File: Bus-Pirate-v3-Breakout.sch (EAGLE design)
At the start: 9 parts

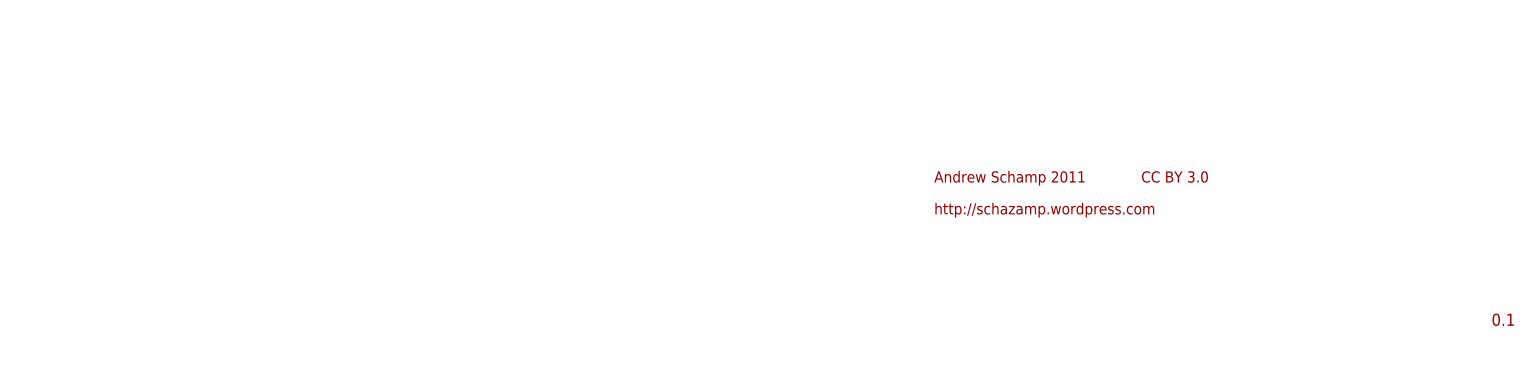
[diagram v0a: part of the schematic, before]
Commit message: Clean up and add panelization config
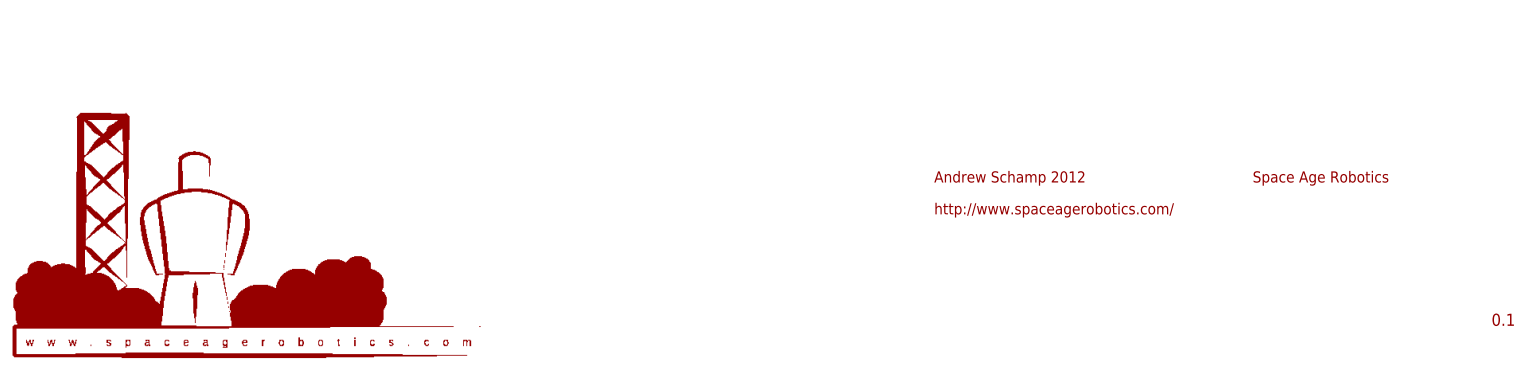
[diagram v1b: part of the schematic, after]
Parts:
- added U$2: LOGO_SPACE_AGE_ROBOTICS0.48*0.27, logos:LOGO_SPACE_AGE_ROBOTICS0.48*0.27
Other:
- note added: "Andrew Schamp 2012"
- note added: "Space Age Robotics"
- note added: "http://www.spaceagerobotics.com/"
- note removed: "Andrew Schamp 2011"
- note removed: "CC BY 3.0"
- note removed: "http://schazamp.wordpress.com"
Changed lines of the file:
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@@
 <grid distance="0.1" unitdist="inch" unit="inch" style="lines" multiple="1" display="no" altdistance="0.01" altunitdist="inch" altunit="inch"/>
 <layers>
-<layer number="1" name="Top" color="4" fill="1" visible="no" active="no"/>
-<layer number="16" name="Bottom" color="1" fill="1" visible="no" active="no"/>
-<layer number="17" name="Pads" color="2" fill="1" visible="no" active="no"/>
-<layer number="18" name="Vias" color="2" fill="1" visible="no" active="no"/>
-<layer number="19" name="Unrouted" color="6" fill="1" visible="no" active="no"/>
-<layer number="20" name="Dimension" color="7" fill="1" visible="no" active="no"/>
-<layer number="21" name="tPlace" color="16" fill="1" visible="no" active="no"/>
-<layer number="22" name="bPlace" color="14" fill="1" visible="no" active="no"/>
-<layer number="23" name="tOrigins" color="15" fill="1" visible="no" active="no"/>
-<layer number="24" name="bOrigins" color="15" fill="1" visible="no" active="no"/>
-<layer number="25" name="tNames" color="7" fill="1" visible="no" active="no"/>
-<layer number="26" name="bNames" color="7" fill="1" visible="no" active="no"/>
-<layer number="27" name="tValues" color="7" fill="1" visible="no" active="no"/>
-<layer number="28" name="bValues" color="7" fill="1" visible="no" active="no"/>
+<layer number="1" name="Top" color="4" fill="1" visible="yes" active="no"/>
+<layer number="16" name="Bottom" color="1" fill="1" visible="yes" active="no"/>
+<layer number="17" name="Pads" color="2" fill="1" visible="yes" active="no"/>
+<layer number="18" name="Vias" color="2" fill="1" visible="yes" active="no"/>
+<layer number="19" name="Unrouted" color="6" fill="1" visible="yes" active="no"/>
+<layer number="20" name="Dimension" color="15" fill="1" visible="yes" active="no"/>
+<layer number="21" name="tPlace" color="16" fill="1" visible="yes" active="no"/>
+<layer number="22" name="bPlace" color="14" fill="1" visible="yes" active="no"/>
+<layer number="23" name="tOrigins" color="15" fill="1" visible="yes" active="no"/>
+<layer number="24" name="bOrigins" color="15" fill="1" visible="yes" active="no"/>
+<layer number="25" name="tNames" color="7" fill="1" visible="yes" active="no"/>
+<layer number="26" name="bNames" color="7" fill="1" visible="yes" active="no"/>
+<layer number="27" name="tValues" color="7" fill="1" visible="yes" active="no"/>
+<layer number="28" name="bValues" color="7" fill="1" visible="yes" active="no"/>
 <layer number="29" name="tStop" color="7" fill="3" visible="no" active="no"/>
 <layer number="30" name="bStop" color="7" fill="6" visible="no" active="no"/>
-<layer number="31" name="tCream" color="11" fill="4" visible="no" active="no"/>
+<layer number="31" name="tCream" color="7" fill="4" visible="no" active="no"/>
 <layer number="32" name="bCream" color="7" fill="5" visible="no" active="no"/>
 <layer number="33" name="tFinish" color="6" fill="3" visible="no" active="no"/>
@@
 <layer number="35" name="tGlue" color="7" fill="4" visible="no" active="no"/>
 <layer number="36" name="bGlue" color="7" fill="5" visible="no" active="no"/>
-<layer number="37" name="tTest" color="7" fill="1" visible="no" active="no"/>
-<layer number="38" name="bTest" color="7" fill="1" visible="no" active="no"/>
+<layer number="37" name="tTest" color="7" fill="1" visible="yes" active="no"/>
+<layer number="38" name="bTest" color="7" fill="1" visible="yes" active="no"/>
 <layer number="39" name="tKeepout" color="4" fill="11" visible="no" active="no"/>
 <layer number="40" name="bKeepout" color="1" fill="11" visible="no" active="no"/>
@@
 <layer number="44" name="Drills" color="7" fill="1" visible="no" active="no"/>
 <layer number="45" name="Holes" color="7" fill="1" visible="no" active="no"/>
-<layer number="46" name="Milling" color="3" fill="1" visible="no" active="no"/>
-<layer number="47" name="Measures" color="7" fill="1" visible="no" active="no"/>
-<layer number="48" name="Document" color="7" fill="1" visible="no" active="no"/>
-<layer number="49" name="Reference" color="13" fill="1" visible="no" active="no"/>
-<layer number="50" name="dxf" color="7" fill="1" visible="no" active="no"/>
-<layer number="51" name="tDocu" color="14" fill="1" visible="no" active="no"/>
-<layer number="52" name="bDocu" color="7" fill="1" visible="no" active="no"/>
-<layer number="53" name="tGND_GNDA" color="7" fill="9" visible="no" active="no"/>
-<layer number="54" name="bGND_GNDA" color="1" fill="9" visible="no" active="no"/>
-<layer number="56" name="wert" color="7" fill="1" visible="no" active="no"/>
+<layer number="46" name="Milling" color="3" fill="1" visible="yes" active="no"/>
+<layer number="47" name="Measures" color="7" fill="1" visible="yes" active="no"/>
+<layer number="48" name="Document" color="7" fill="1" visible="yes" active="no"/>
+<layer number="49" name="Reference" color="7" fill="1" visible="yes" active="no"/>
+<layer number="50" name="dxf" color="7" fill="1" visible="yes" active="no"/>
+<layer number="51" name="tDocu" color="6" fill="1" visible="yes" active="no"/>
+<layer number="52" name="bDocu" color="7" fill="1" visible="yes" active="no"/>
+<layer number="53" name="tGND_GNDA" color="7" fill="9" visible="yes" active="no"/>
+<layer number="54" name="bGND_GNDA" color="1" fill="9" visible="yes" active="no"/>
+<layer number="56" name="wert" color="7" fill="1" visible="yes" active="no"/>
 <layer number="91" name="Nets" color="2" fill="1" visible="yes" active="yes"/>
 <layer number="92" name="Busses" color="1" fill="1" visible="yes" active="yes"/>
@@
 <layer number="106" name="bPlate" color="7" fill="1" visible="yes" active="yes"/>
 <layer number="107" name="Crop" color="7" fill="1" visible="yes" active="yes"/>
+<layer number="108" name="centerline" color="7" fill="1" visible="no" active="yes"/>
 <layer number="116" name="Patch_BOT" color="9" fill="4" visible="yes" active="yes"/>
 <layer number="121" name="_tsilk" color="7" fill="1" visible="yes" active="yes"/>
 <layer number="122" name="_bsilk" color="7" fill="1" visible="yes" active="yes"/>
 <layer number="125" name="_tNames" color="7" fill="1" visible="no" active="yes"/>
+<layer number="131" name="prix" color="7" fill="1" visible="no" active="yes"/>
+<layer number="132" name="test" color="7" fill="1" visible="no" active="yes"/>
 <layer number="144" name="Drill_legend" color="7" fill="1" visible="no" active="yes"/>
 <layer number="151" name="HeatSink" color="7" fill="1" visible="yes" active="yes"/>
@@
 <part name="PULLUP" library="SparkFun" deviceset="M02" device="LOCK"/>
 <part name="JTAG" library="SparkFun-Connectors" deviceset="M06" device="LOCK"/>
+<part name="U$2" library="logos" deviceset="LOGO_SPACE_AGE_ROBOTICS" device="0.48*0.27"/>
 </parts>
 <sheets>
@@
 <plain>
 <text x="144.78" y="-43.18" size="1.9304" layer="94">0.1</text>
-<text x="55.88" y="-20.32" size="1.778" layer="94">Andrew Schamp 2011</text>
-<text x="55.88" y="-25.4" size="1.778" layer="94">http://schazamp.wordpress.com</text>
-<text x="88.9" y="-20.32" size="1.778" layer="94">CC BY 3.0</text>
+<text x="55.88" y="-20.32" size="1.778" layer="94">Andrew Schamp 2012</text>
+<text x="55.88" y="-25.4" size="1.778" layer="94">http://www.spaceagerobotics.com/</text>
+<text x="106.68" y="-20.32" size="1.778" layer="94">Space Age Robotics</text>
 </plain>
 <instances>
@@
 <instance part="PULLUP" gate="G$1" x="20.32" y="68.58"/>
 <instance part="JTAG" gate="G$1" x="-5.08" y="86.36"/>
+<instance part="U$2" gate="G$1" x="-91.44" y="-48.26"/>
 </instances>
 <busses>
